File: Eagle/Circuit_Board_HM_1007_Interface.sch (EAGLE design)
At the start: 18 parts

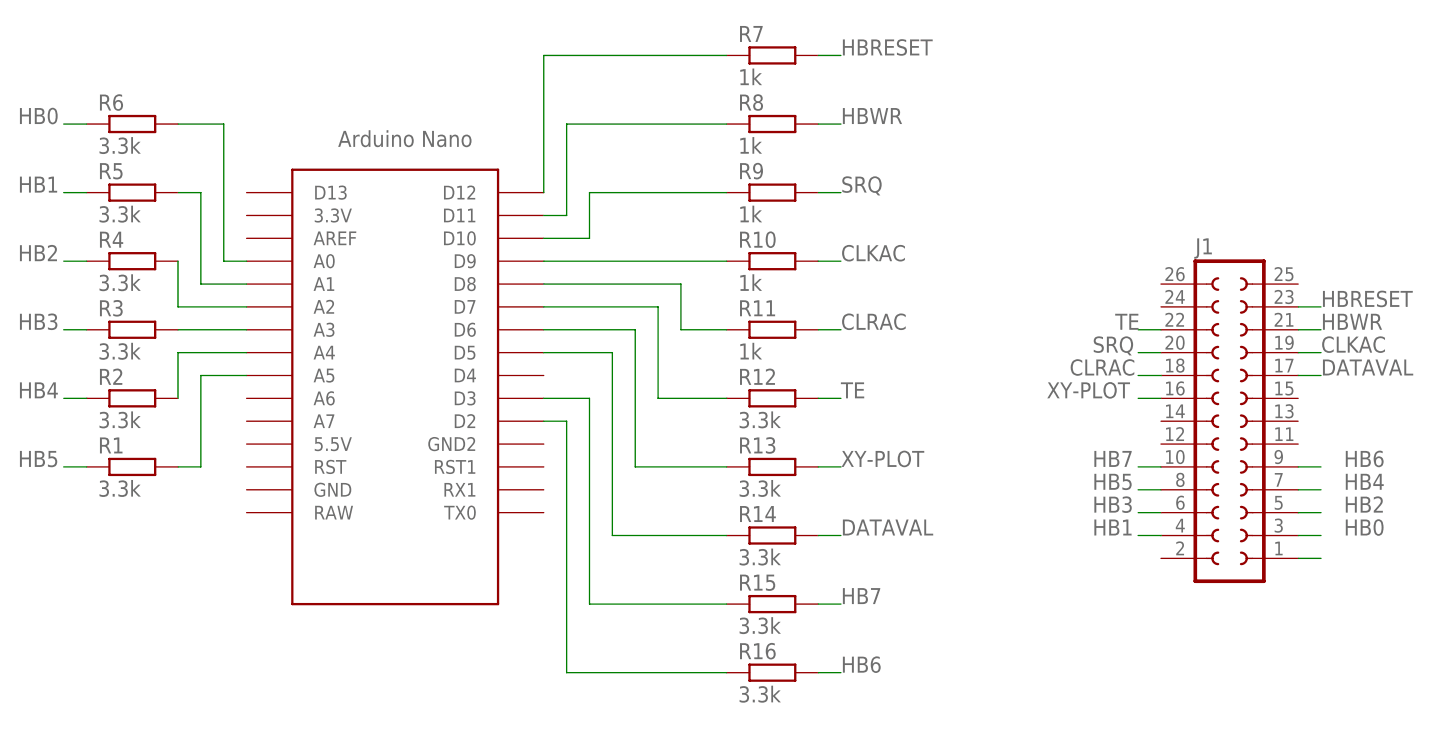
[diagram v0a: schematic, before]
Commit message: fixed missing GND label in schematic
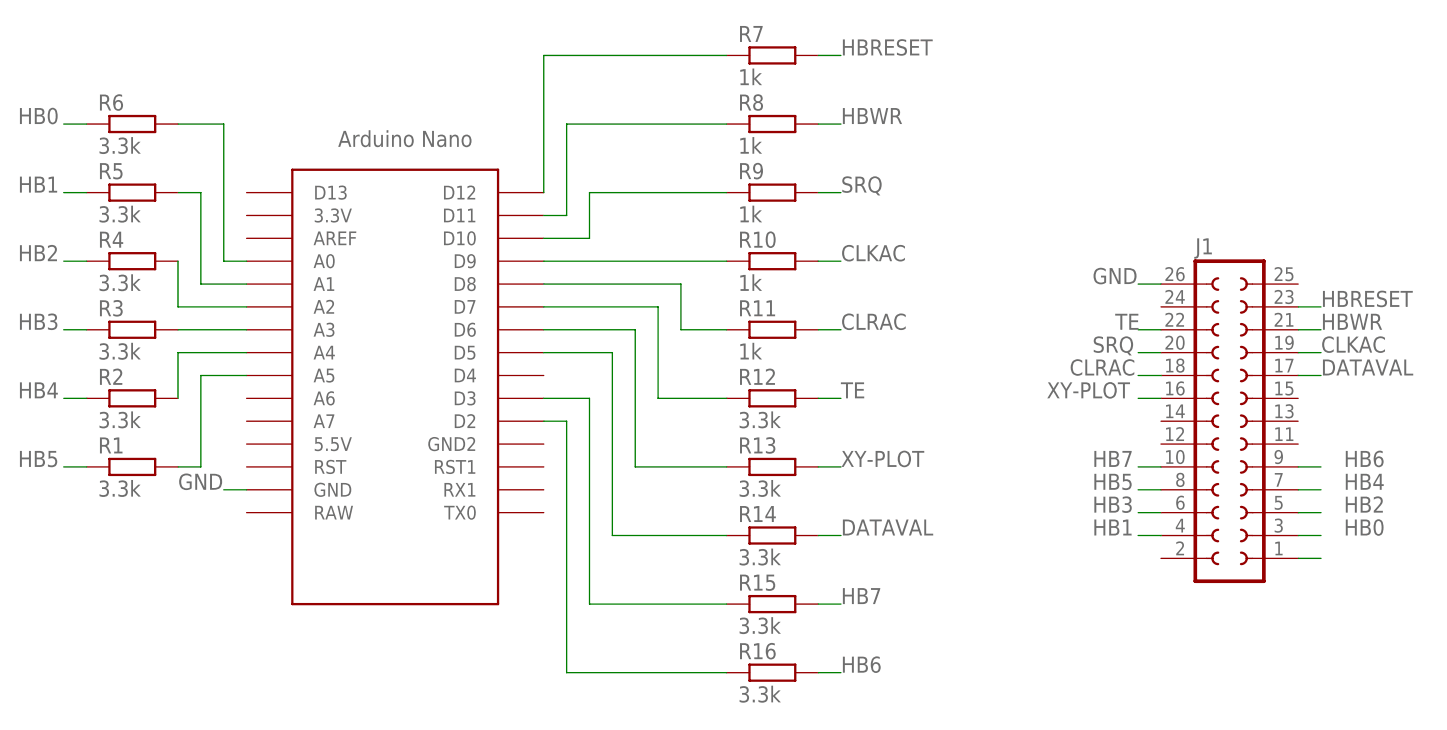
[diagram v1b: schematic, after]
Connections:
- new net GND: J1.26, U$1.GND
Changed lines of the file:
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@@
 <setting verticaltext="up"/>
 </settings>
-<grid distance="0.1" unitdist="inch" unit="inch" style="lines" multiple="1" display="yes" altdistance="0.01" altunitdist="inch" altunit="inch"/>
+<grid distance="0.1" unitdist="inch" unit="inch" style="lines" multiple="1" display="no" altdistance="0.01" altunitdist="inch" altunit="inch"/>
 <layers>
 <layer number="1" name="Top" color="4" fill="1" visible="no" active="no"/>
@@
 </segment>
 </net>
+<net name="GND" class="0">
+<segment>
+<pinref part="U$1" gate="G$1" pin="GND"/>
+<wire x1="20.32" y1="40.64" x2="17.78" y2="40.64" width="0.1524" layer="91"/>
+<label x="12.7" y="40.64" size="1.778" layer="95"/>
+</segment>
+<segment>
+<pinref part="J1" gate="G$1" pin="26"/>
+<wire x1="121.92" y1="63.5" x2="119.38" y2="63.5" width="0.1524" layer="91"/>
+<label x="114.3" y="63.5" size="1.778" layer="95"/>
+</segment>
+</net>
